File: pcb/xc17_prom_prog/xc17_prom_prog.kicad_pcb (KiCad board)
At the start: 2 copper layers, 123 x 95 mm, 240 parts, among them J1 Conn_02x02_Odd_Even, J2 USB_B_Micro, J3 Conn_02x20_Odd_Even, Q1 BC850, Q10 BC850, Q11 BC850, Q12 BC850, Q2 BC850, Q3 BC850, Q4 IRLML9301, Q5 IRLML9301, Q6 IRLML9301, Q7 IRLML9301, Q8 IRLML9301, Q9 IRLML9301, U1 W25Q32JVSSIM, U10 LM317, U11 MC33063AD, U12 LM317, U13 LM317, U14 SN74LVC8T245, U15 SN74LVC8T245, U16 SN74LVC8T245, U17 XC17xxx, U2 LT3030, U3 ICE40HX1K-VQ100, U4 93LC56B, U5 FT2232HL, U6 LM317, U7 LM317, U8 MC33063AD, U9 LM317, X1 12M

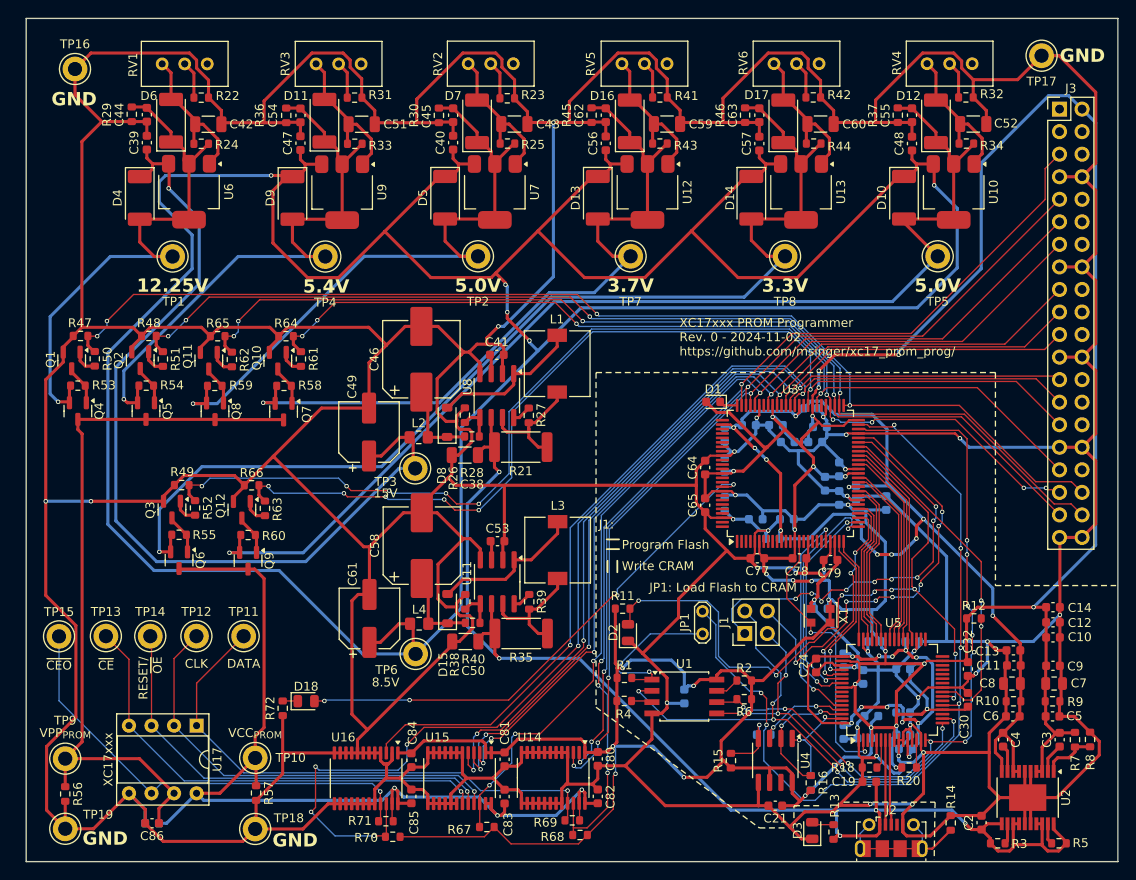
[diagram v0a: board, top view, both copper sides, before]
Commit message: Fix MOSFETs
 * Block MOSFET body diodes by placing two MOSFETs in anti series.
 * Connect PROM LED to pin header.
 * Add transistors to actively pull PROM VCC and VPP low.
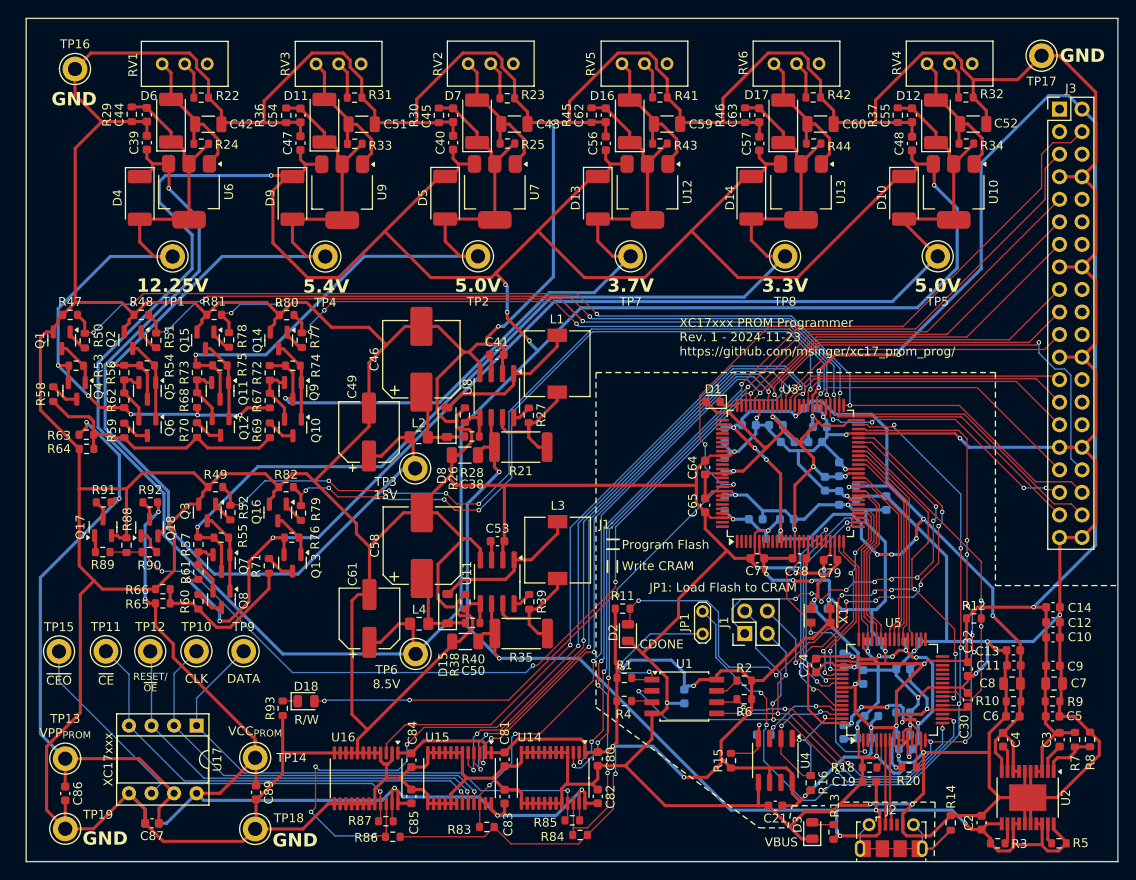
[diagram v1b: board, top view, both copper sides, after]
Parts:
- removed the R64 at (119.3, 75.8)
- removed the R66 at (115.4, 92.6)
- removed the TP10 at (115.8, 123.3)
- removed the TP9 at (94.4, 123.4)
- added C86: 100n, Capacitor_SMD:C_0603_1608Metric, F.Cu at (94.4, 127.3)
- added C89: 100n, Capacitor_SMD:C_0603_1608Metric, F.Cu at (115.9, 127.2)
- added Q13: IRLML9301, Package_TO_SOT_SMD:SOT-23, F.Cu at (120.0, 101.3)
- added Q14: BC850, Package_TO_SOT_SMD:SOT-23, F.Cu at (118.5, 76.3)
- added Q15: BC850, Package_TO_SOT_SMD:SOT-23, F.Cu at (110.2, 76.3)
- added Q16: BC850, Package_TO_SOT_SMD:SOT-23, F.Cu at (118.3, 95.7)
- added Q17: BC850, Package_TO_SOT_SMD:SOT-23, F.Cu at (98.7, 97.3)
- added Q18: BC850, Package_TO_SOT_SMD:SOT-23, F.Cu at (103.9, 97.4)
- added R56: 1M, Resistor_SMD:R_0603_1608Metric, F.Cu at (101.0, 79.9)
- added R57: 1M, Resistor_SMD:R_0603_1608Metric, F.Cu at (109.4, 99.3)
- added R67: 1M, Resistor_SMD:R_0603_1608Metric, F.Cu at (117.5, 83.0)
- added R68: 1M, Resistor_SMD:R_0603_1608Metric, F.Cu at (109.2, 83.0)
- added R69: 0, Resistor_SMD:R_0603_1608Metric, F.Cu at (117.5, 86.4)
- added R70: 0, Resistor_SMD:R_0603_1608Metric, F.Cu at (109.2, 86.4)
- added R71: 0, Resistor_SMD:R_0603_1608Metric, F.Cu at (117.3, 101.7)
- added R72: 1M, Resistor_SMD:R_0603_1608Metric, F.Cu at (117.5, 79.9)
- added R73: 1M, Resistor_SMD:R_0603_1608Metric, F.Cu at (109.2, 79.9)
- added R74: 2.05k, Resistor_SMD:R_0603_1608Metric, F.Cu at (120.0, 79.1)
- added R75: 2.05k, Resistor_SMD:R_0603_1608Metric, F.Cu at (111.8, 79.1)
- added R76: 2.05k, Resistor_SMD:R_0603_1608Metric, F.Cu at (119.9, 98.5)
- added R77: 422, Resistor_SMD:R_0603_1608Metric, F.Cu at (121.0, 76.2)
- added R78: 422, Resistor_SMD:R_0603_1608Metric, F.Cu at (112.8, 76.2)
- added R79: 422, Resistor_SMD:R_0603_1608Metric, F.Cu at (121.0, 95.7)
- added R80: 10k, Resistor_SMD:R_0603_1608Metric, F.Cu at (119.3, 73.4)
- added R81: 10k, Resistor_SMD:R_0603_1608Metric, F.Cu at (111.2, 73.4)
- added R82: 10k, Resistor_SMD:R_0603_1608Metric, F.Cu at (119.3, 92.8)
- added R88: 10k, Resistor_SMD:R_0603_1608Metric, F.Cu at (101.3, 99.3)
- added R89: 422, Resistor_SMD:R_0603_1608Metric, F.Cu at (98.6, 100.1)
- added R90: 422, Resistor_SMD:R_0603_1608Metric, F.Cu at (103.9, 100.1)
- added R91: 0, Resistor_SMD:R_0603_1608Metric, F.Cu at (98.7, 94.5)
- added R92: 0, Resistor_SMD:R_0603_1608Metric, F.Cu at (104.0, 94.5)
- added TP13: VPP_{PROM}, TestPoint:TestPoint_Keystone_5010-5014_Multipurpose, F.Cu at (94.4, 123.4)
- added TP14: VCC_{PROM}, TestPoint:TestPoint_Keystone_5010-5014_Multipurpose, F.Cu at (115.8, 123.3)
- Q10, Q11, Q12: value BC850 -> IRLML9301
- R11: value 665 -> 2.05k
- R13: value 1k -> 2.05k
- R58, R59, R60: value 2.05k -> 0
- R61, R62: value 422 -> 1M
- R63: value 422 -> 0
- R65: value 10k -> 0
- R93: renamed from R72; value 1k -> 2.05k
- moved R64 39.0 mm to (96.8, 88.5), turned to 180 degrees
- moved R65 30.7 mm to (105.4, 105.9), turned to 0 degrees
- moved R61 26.6 mm to (109.4, 102.4)
- moved R58 26.0 mm to (93.0, 82.3), turned to -90 degrees
- moved R66 25.3 mm to (105.4, 104.3), turned to 180 degrees
- moved R63 21.8 mm to (96.8, 86.9), turned to 0 degrees
- moved Q8 21.2 mm to (112.0, 105.5)
- moved Q9 19.8 mm to (120.0, 82.0)
- moved Q7 18.4 mm to (112.0, 101.4)
- moved Q6 15.4 mm to (103.7, 86.1)
- moved R62 13.0 mm to (101.0, 83.0)
- moved R59 11.4 mm to (101.0, 86.4), turned to -90 degrees
- moved Q12 9.63 mm to (111.9, 86.0)
- moved R60 9.38 mm to (109.4, 105.7), turned to -90 degrees
- moved Q10 7.71 mm to (120.0, 86.1)
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- renumbered C86 to C87, C87 to C88, R56 to R64, R57 to R66, R67 to R83, R68 to R84, R69 to R85, R70 to R86, R71 to R87, TP12 to TP10, TP13 to TP11, TP14 to TP12, TP11 to TP9
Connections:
- J3 pad 34: unconnected-(J3-Pin_34-Pad34) -> /FPGA/SELECT_GND
- J3 pad 4: unconnected-(J3-Pin_4-Pad4) -> /FPGA/PROM_LED
- Q10 pad 1: Net-(Q10-B) -> Net-(Q10-G)
- Q10 pad 2: GND -> Net-(Q10-S)
- Q10 pad 3: Net-(Q10-C) -> Net-(Q10-D)
- Q11 pad 1: Net-(Q11-B) -> Net-(Q11-G)
- Q11 pad 2: GND -> Net-(Q11-S)
- Q11 pad 3: Net-(Q11-C) -> +5VP
- Q12 pad 1: Net-(Q12-B) -> Net-(Q11-G)
- Q12 pad 2: GND -> Net-(Q11-S)
- Q12 pad 3: Net-(Q12-C) -> Net-(Q12-D)
- Q4 pad 3: VPP_{PROM} -> Net-(Q4-D)
- Q5 pad 2: +5V4P -> Net-(Q5-S)
- Q5 pad 3: VPP_{PROM} -> +5V4P
- Q6 pad 1: Net-(Q3-C) -> Net-(Q2-C)
- Q6 pad 2: +3V3C -> Net-(Q5-S)
- Q6 pad 3: VCC_{PROM} -> Net-(Q6-D)
- Q7 pad 1: Net-(Q10-C) -> Net-(Q3-C)
- Q7 pad 2: +3V7P -> Net-(Q7-S)
- Q7 pad 3: VPP_{PROM} -> +3V3C
- Q8 pad 1: Net-(Q11-C) -> Net-(Q3-C)
- Q8 pad 2: +5VP -> Net-(Q7-S)
- Q8 pad 3: VPP_{PROM} -> Net-(Q8-D)
- Q9 pad 1: Net-(Q12-C) -> Net-(Q10-G)
- Q9 pad 2: +5VC -> Net-(Q10-S)
- Q9 pad 3: VCC_{PROM} -> +3V7P
- R58 pad 1: +3V7P -> Net-(Q4-D)
- R58 pad 2: Net-(Q10-C) -> Net-(R58-Pad2)
- R59 pad 1: +5VP -> Net-(Q6-D)
- R59 pad 2: Net-(Q11-C) -> Net-(R58-Pad2)
- R60 pad 1: +5VC -> Net-(Q8-D)
- R60 pad 2: Net-(Q12-C) -> Net-(R60-Pad2)
- R61 pad 1: Net-(Q10-B) -> +5VC
- R61 pad 2: /FPGA/SELECT_VPP_3V7 -> Net-(Q7-S)
- R62 pad 1: Net-(Q11-B) -> +12V25P
- R62 pad 2: /FPGA/SELECT_VPP_5V -> Net-(Q5-S)
- R63 pad 1: Net-(Q12-B) -> VPP_{PROM}
- R63 pad 2: /FPGA/SELECT_VCC_5V -> Net-(R58-Pad2)
- R64 pad 1: VPP_{PROM} -> Net-(R58-Pad2)
- R65 pad 1: /FPGA/SELECT_VPP_5V -> VCC_{PROM}
- R65 pad 2: GND -> Net-(R60-Pad2)
- R66 pad 1: VCC_{PROM} -> Net-(R60-Pad2)
- U3 pad 65: unconnected-(U3B-IOR_64-Pad65) -> /FPGA/SELECT_GND
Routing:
- net /FPGA/SELECT_GND: track 0.00 -> 149.3 mm, vias 0 -> 5
- net /FPGA/PROM_LED: track 59.1 -> 127.8 mm, vias 4 -> 5
- net GND: track 1271.9 -> 1303.0 mm, vias 31 -> 29
- net Net-(R58-Pad2): track 0.00 -> 30.5 mm
- net +12V25P: track 62.3 -> 84.7 mm, vias 1 -> 5
- net Net-(R60-Pad2): track 0.00 -> 17.4 mm
- net VPP_{PROM}: track 83.5 -> 68.3 mm, vias 0 -> 2
- net +5VC: track 128.0 -> 142.1 mm, vias 1 -> 3
- net Net-(Q11-G): track 0.00 -> 9.32 mm
- net Net-(Q10-G): track 0.00 -> 9.29 mm
- net Net-(Q7-S): track 0.00 -> 6.89 mm
- net Net-(Q5-S): track 0.00 -> 6.86 mm
- net Net-(Q11-S): track 0.00 -> 6.85 mm
- net Net-(Q10-S): track 0.00 -> 6.85 mm
- net /FPGA/SELECT_VPP_5V: track 111.7 -> 117.0 mm
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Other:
- board text added: "CDONE"
- board text added: "R/W"
- board text added: "VBUS"

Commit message: Implement more precise voltage controls
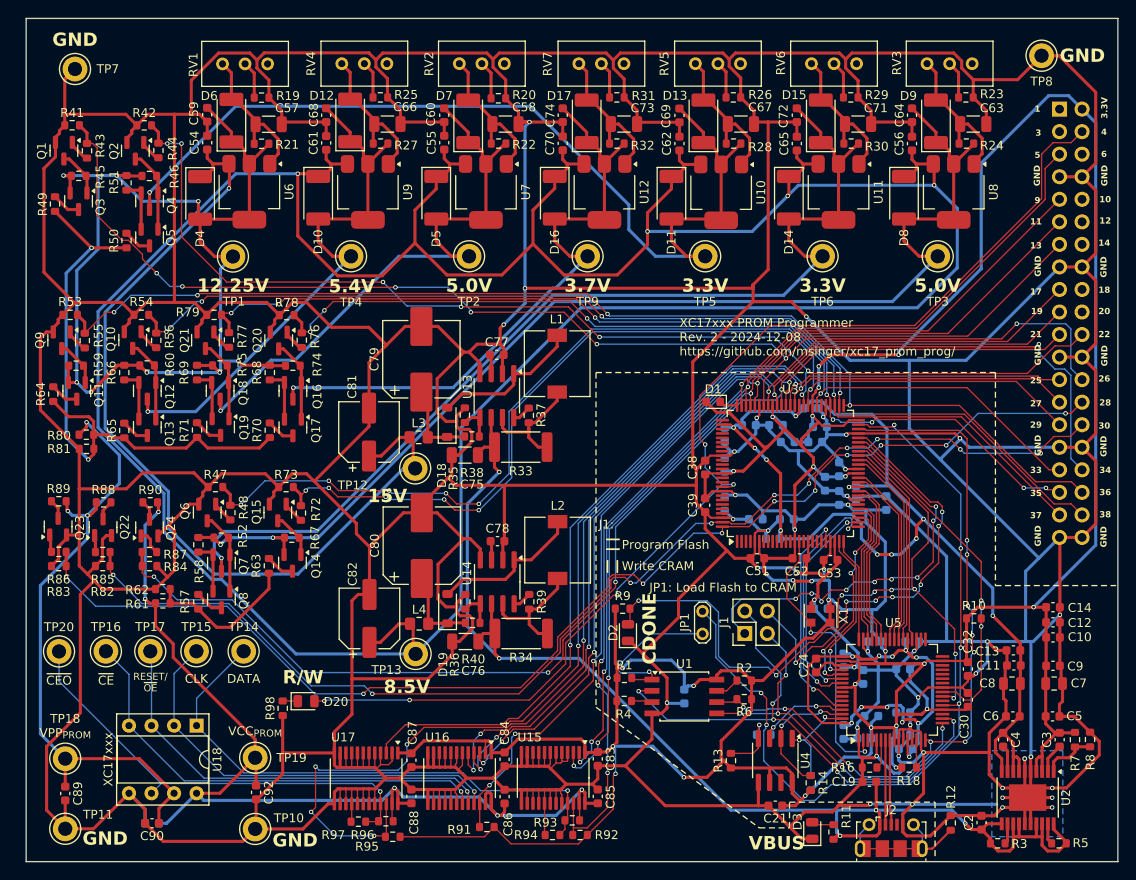
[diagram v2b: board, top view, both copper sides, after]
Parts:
- removed the R10 at (201.2, 116.9)
- removed the R29 at (101.9, 50.8)
- removed the R30 at (136.5, 50.9)
- removed the R36 at (119.3, 50.9)
- removed the R37 at (188.2, 50.9)
- removed the R56 at (101.0, 79.9)
- removed the R57 at (109.4, 99.3)
- removed the R72 at (117.5, 79.9)
- removed the R73 at (109.2, 79.9)
- removed the R9 at (205.6, 116.9)
- added C62: 100n, Capacitor_SMD:C_0603_1608Metric, F.Cu at (163.6, 54.1)
- added C67: 10µ 16V, Capacitor_SMD:C_1206_3216Metric, F.Cu at (170.5, 51.9)
- added C69: 1µ 16V, Capacitor_SMD:C_0603_1608Metric, F.Cu at (163.6, 50.9)
- added D11: 1N4002, Diode_SMD:D_MELF, F.Cu at (162.7, 60.2)
- added D13: 1N4002, Diode_SMD:D_MELF, F.Cu at (166.3, 51.6)
- added Q1: BC850, Package_TO_SOT_SMD:SOT-23, F.Cu at (94.2, 54.9)
- added Q2: BC850, Package_TO_SOT_SMD:SOT-23, F.Cu at (102.3, 54.9)
- added Q23: BC850, Package_TO_SOT_SMD:SOT-23, F.Cu at (93.6, 97.3)
- added Q3: IRLML9301, Package_TO_SOT_SMD:SOT-23, F.Cu at (95.9, 60.6)
- added Q4: IRLML9301, Package_TO_SOT_SMD:SOT-23, F.Cu at (103.9, 60.6)
- added Q5: IRLML9301, Package_TO_SOT_SMD:SOT-23, F.Cu at (103.9, 64.7)
- added R26: 340, Resistor_SMD:R_0603_1608Metric, F.Cu at (169.7, 48.9)
- added R28: 240, Resistor_SMD:R_0603_1608Metric, F.Cu at (169.7, 54.1)
- added R41: 10k, Resistor_SMD:R_0603_1608Metric, F.Cu at (95.2, 52.0)
- added R42: 10k, Resistor_SMD:R_0603_1608Metric, F.Cu at (103.3, 52.0)
- added R43: 422, Resistor_SMD:R_0603_1608Metric, F.Cu at (96.8, 54.9)
- added R44: 422, Resistor_SMD:R_0603_1608Metric, F.Cu at (104.9, 54.9)
- added R49: 1.5, Resistor_SMD:R_0603_1608Metric, F.Cu at (93.2, 60.9)
- added R50: 0, Resistor_SMD:R_0603_1608Metric, F.Cu at (101.3, 65.0)
- added R51: 1M, Resistor_SMD:R_0603_1608Metric, F.Cu at (101.3, 58.5)
- added R82: 10k, Resistor_SMD:R_0603_1608Metric, F.Cu at (98.6, 101.7)
- added R83: 10k, Resistor_SMD:R_0603_1608Metric, F.Cu at (93.7, 101.7)
- added R86: 422, Resistor_SMD:R_0603_1608Metric, F.Cu at (93.7, 100.1)
- added R89: 1.5, Resistor_SMD:R_0603_1608Metric, F.Cu at (93.7, 94.4)
- added R94: 100k, Resistor_SMD:R_0603_1608Metric, F.Cu at (149.3, 132.0)
- added R97: 100k, Resistor_SMD:R_0603_1608Metric, F.Cu at (127.4, 130.5)
- added RV5: 100, Potentiometer_THT:Potentiometer_Bourns_3296W_Vertical, F.Cu at (165.4, 45.1)
- added TP5: 3.3V, TestPoint:TestPoint_Keystone_5010-5014_Multipurpose, F.Cu at (166.5, 66.8)
- added U10: LM317, Package_TO_SOT_SMD:SOT-223-3_TabPin2, F.Cu at (168.3, 59.6)
- R45, R46: value 240 -> 2.05k
- moved R46 67.5 mm to (103.9, 57.8), turned to 0 degrees
- moved R45 58.2 mm to (95.9, 57.7), turned to 0 degrees
- moved D6 6.80 mm to (113.1, 51.5)
- moved RV1 6.80 mm to (112.1, 45.1)
- moved C54 6.80 mm to (110.4, 54.0)
- moved C57 6.80 mm to (117.3, 51.9)
- moved C59 6.80 mm to (110.4, 50.9)
- moved D4 6.80 mm to (109.6, 60.2)
- moved R19 6.80 mm to (116.5, 48.9)
- moved R21 6.80 mm to (116.5, 54.1)
- moved TP1 6.80 mm to (113.3, 66.8)
- moved U6 6.80 mm to (115.1, 59.5)
- moved C70 4.85 mm to (150.4, 54.1)
- moved C74 4.85 mm to (150.4, 50.9)
- moved C73 4.85 mm to (157.3, 51.9)
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- renumbered C64 to C38, C65 to C39, C66 to C40, C67 to C41, C68 to C42, C69 to C43, C70 to C44, C71 to C45, C72 to C46, C73 to C47, C74 to C48, C75 to C49, C76 to C50, C77 to C51, C78 to C52, C79 to C53, C39 to C54, C40 to C55, C48 to C56, C42 to C57, C43 to C58, C44 to C59, C45 to C60, C47 to C61, C52 to C63, C55 to C64, C57 to C65, C51 to C66, C54 to C68, C56 to C70, C60 to C71, C63 to C72, C59 to C73, C62 to C74, C38 to C75, C50 to C76, C41 to C77, C53 to C78, C46 to C79, C58 to C80, C49 to C81, C61 to C82, C80 to C83, C81 to C84, C82 to C85, C83 to C86, C84 to C87, C85 to C88, C86 to C89, C87 to C90, C88 to C91, C89 to C92, D9 to D10, D11 to D12, D17 to D15, D13 to D16, D16 to D17, D8 to D18, D15 to D19, D18 to D20, D10 to D8, D12 to D9, L3 to L2, L2 to L3, Q2 to Q10, Q4 to Q11, Q5 to Q12, Q6 to Q13, Q13 to Q14, Q16 to Q15, Q9 to Q16, Q10 to Q17, Q11 to Q18, Q12 to Q19, Q14 to Q20, Q15 to Q21, Q17 to Q22, Q18 to Q24, Q3 to Q6, Q1 to Q9, R12 to R10, R13 to R11, R14 to R12, R15 to R13, R16 to R14, R17 to R15, R18 to R16, R19 to R17, R20 to R18, R22 to R19, R23 to R20, R24 to R21, R25 to R22, R32 to R23, R34 to R24, R31 to R25, R33 to R27, R42 to R29, R44 to R30, R41 to R31, R43 to R32, R21 to R33, R35 to R34, R26 to R35, R38 to R36, R27 to R37, R28 to R38, R49 to R47, R52 to R48, R55 to R52, R47 to R53, R48 to R54, R50 to R55, R51 to R56, R60 to R57, R61 to R58, R53 to R59, R54 to R60, R65 to R61, R66 to R62, R71 to R63, R58 to R64, R59 to R65, R62 to R66, R76 to R67, R67 to R68, R68 to R69, R69 to R70, R70 to R71, R79 to R72, R82 to R73, R77 to R76, R78 to R77, R80 to R78, R81 to R79, R63 to R80, R64 to R81, R88 to R84, R89 to R85, R90 to R87, R91 to R88, R11 to R9, R92 to R90, R83 to R91, R84 to R92, R85 to R93, R86 to R95, R87 to R96, R93 to R98, RV4 to RV3, RV3 to RV4, RV5 to RV7, TP18 to TP10, TP19 to TP11, TP3 to TP12, TP6 to TP13, TP9 to TP14, TP10 to TP15, TP11 to TP16, TP12 to TP17, TP13 to TP18, TP14 to TP19, TP15 to TP20, TP5 to TP3, TP8 to TP6, TP16 to TP7, TP17 to TP8, TP7 to TP9, U13 to U11, U8 to U13, U11 to U14, U14 to U15, U15 to U16, U16 to U17, U17 to U18, U10 to U8
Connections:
- J3 pad 22: unconnected-(J3-Pin_22-Pad22) -> /FPGA/SELECT_VPP_3V3
- J3 pad 26: unconnected-(J3-Pin_26-Pad26) -> /FPGA/SELECT_VPP_12V25_WEAK
- J3 pad 28: unconnected-(J3-Pin_28-Pad28) -> /FPGA/SELECT_VPP_GND_WEAK
- J3 pad 30: unconnected-(J3-Pin_30-Pad30) -> /FPGA/SELECT_VPP_GND
- J3 pad 34: /FPGA/SELECT_GND -> /FPGA/SELECT_VCC_GND
- R45 pad 1: +3V7P -> +12V25P
- R45 pad 2: GND -> Net-(Q1-C)
- R46 pad 1: +3V3C -> +12V25P
- R46 pad 2: GND -> Net-(Q2-C)
- R52 pad 1: +3V3C -> +5VC
- R60 pad 1: +5V4P -> +12V25P
- R74 pad 1: +3V7P -> +12V25P
- R75 pad 1: +5VP -> +12V25P
- R84 pad 1: /FPGA/SELECT_GND -> /FPGA/SELECT_VCC_GND
- R85 pad 1: /FPGA/SELECT_GND -> /FPGA/SELECT_VPP_GND
- R87 pad 1: /FPGA/SELECT_GND -> /FPGA/SELECT_VCC_GND
- U3 pad 100: unconnected-(U3A-IOT_95-Pad100) -> /FPGA/SELECT_VPP_GND_WEAK
- U3 pad 60: unconnected-(U3B-IOR_59-Pad60) -> /FPGA/SELECT_VPP_3V3
- U3 pad 65: /FPGA/SELECT_GND -> /FPGA/SELECT_VCC_GND
- U3 pad 69: unconnected-(U3B-IOR_68-Pad69) -> /FPGA/SELECT_VPP_12V25_WEAK
- U3 pad 99: unconnected-(U3A-IOT_93-Pad99) -> /FPGA/SELECT_VPP_GND
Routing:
- net GND: track 1303.0 -> 1606.1 mm, vias 29 -> 39
- net /FPGA/SELECT_GND: track 149.3 -> 0.00 mm, vias 5 -> 0
- net /FPGA/SELECT_VCC_GND: track 0.00 -> 147.9 mm, vias 0 -> 5
- net /FPGA/SELECT_VPP_12V25_WEAK: track 0.00 -> 142.6 mm, vias 0 -> 7
- net /FPGA/SELECT_VPP_GND_WEAK: track 0.00 -> 139.9 mm, vias 0 -> 10
- net /FPGA/SELECT_VPP_GND: track 0.00 -> 133.9 mm, vias 0 -> 10
- net /FPGA/SELECT_VPP_3V3: track 0.00 -> 129.4 mm, vias 0 -> 7
- net +3V3P: track 0.00 -> 108.0 mm, vias 0 -> 1
- net +12V25P: track 84.7 -> 124.4 mm, vias 5 -> 8
- net Net-(R49-Pad2): track 30.5 -> 67.8 mm, vias 0 -> 2
- net +8V5: track 378.9 -> 360.4 mm, vias 5 -> 4
- net Net-(D13-A): track 0.00 -> 17.3 mm
- net +3V7P: track 85.1 -> 71.4 mm
- net +5VC: track 142.1 -> 131.1 mm, vias 3 -> 2
- net Net-(Q2-C): track 0.00 -> 9.31 mm
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- added copper zone on B.Cu, net GND
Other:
- board text added: "1"
- board text added: "10"
- board text added: "11"
- board text added: "12"
- board text added: "13"
- board text added: "14"
- board text added: "17"
- board text added: "18"
- board text added: "19"
- board text added: "20"
- board text added: "21"
- board text added: "22"
- board text added: "25"
- board text added: "26"
- board text added: "27"
- board text added: "28"
- board text added: "29"
- board text added: "3"
- board text added: "3.3V"
- board text added: "30"
- board text added: "33"
- board text added: "34"
- board text added: "35"
- board text added: "36"
- board text added: "37"
- board text added: "38"
- board text added: "4"
- board text added: "5"
- board text added: "6"
- board text added: "9"
- board text added: "GND"
- board text added: "to iCE40-HX8K Breakout Board J2"

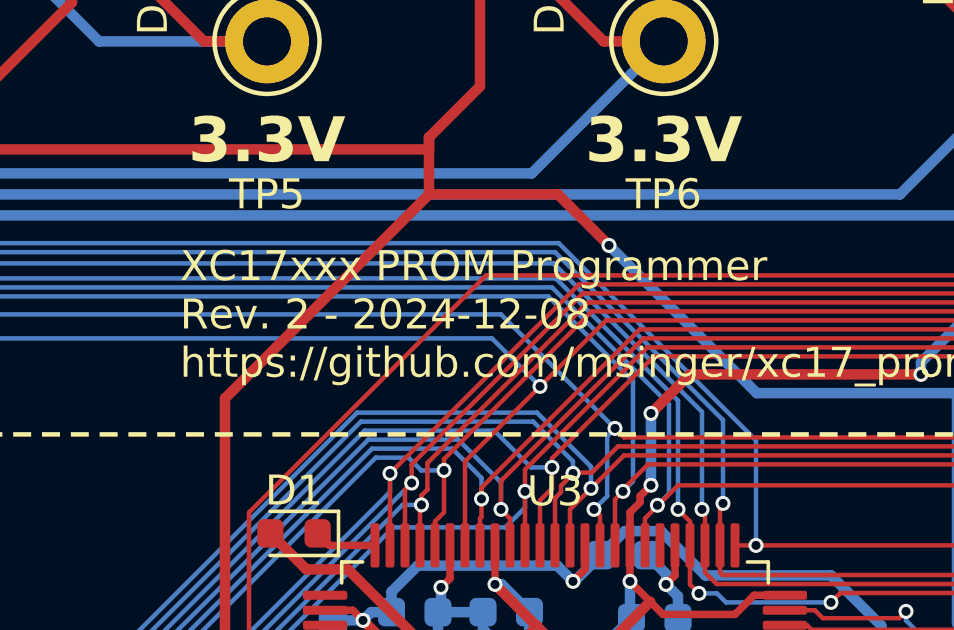
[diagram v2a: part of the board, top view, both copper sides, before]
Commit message: Fix voltage over-/under-shots
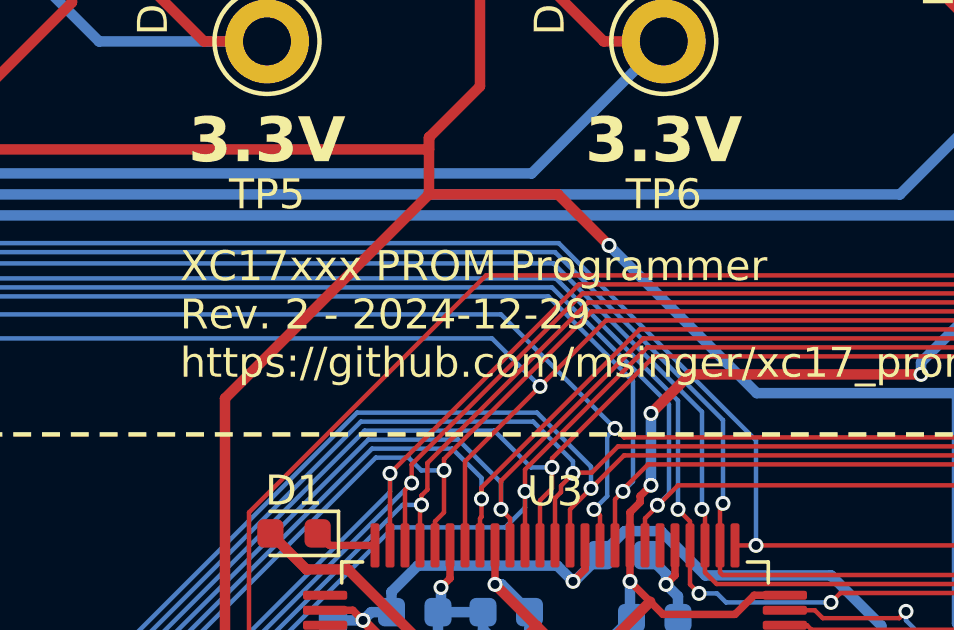
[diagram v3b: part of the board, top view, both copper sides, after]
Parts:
- R50, R57, R63, R65, R70, R71: value 0 -> 1.5
- R89: value 1.5 -> 47
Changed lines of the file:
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@@
 	(title_block
 		(title "XC17xxx PROM Programmer")
-		(date "2024-12-08")
+		(date "2024-12-29")
 		(rev "2")
 		(company "CC-BY-SA-4.0 Michael Singer")
@@
 			)
 		)
-		(property "Value" "0"
+		(property "Value" "1.5"
 			(at 0 1.43 90)
 			(layer "F.Fab")
@@
 			)
 		)
-		(property "Value" "1.5"
+		(property "Value" "47"
 			(at 0 1.43 0)
 			(layer "F.Fab")
@@
 			)
 		)
-		(property "Value" "0"
+		(property "Value" "1.5"
 			(at 0 -1.4 90)
 			(layer "F.Fab")
@@
 			)
 		)
-		(property "Value" "0"
+		(property "Value" "1.5"
 			(at 0 1.43 90)
 			(layer "F.Fab")
@@
 			)
 		)
-		(property "Value" "0"
+		(property "Value" "1.5"
 			(at -0.025 -1.4 90)
 			(layer "F.Fab")
@@
 			)
 		)
-		(property "Value" "0"
+		(property "Value" "1.5"
 			(at 0 1.43 90)
 			(layer "F.Fab")
@@
 			)
 		)
-		(property "Value" "0"
+		(property "Value" "1.5"
 			(at 0.075 -1.4 90)
 			(layer "F.Fab")
